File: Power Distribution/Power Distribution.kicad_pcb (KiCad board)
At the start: 16 copper layers, 20 parts, among them IC3 PCM5102 Audio Stereo DAC

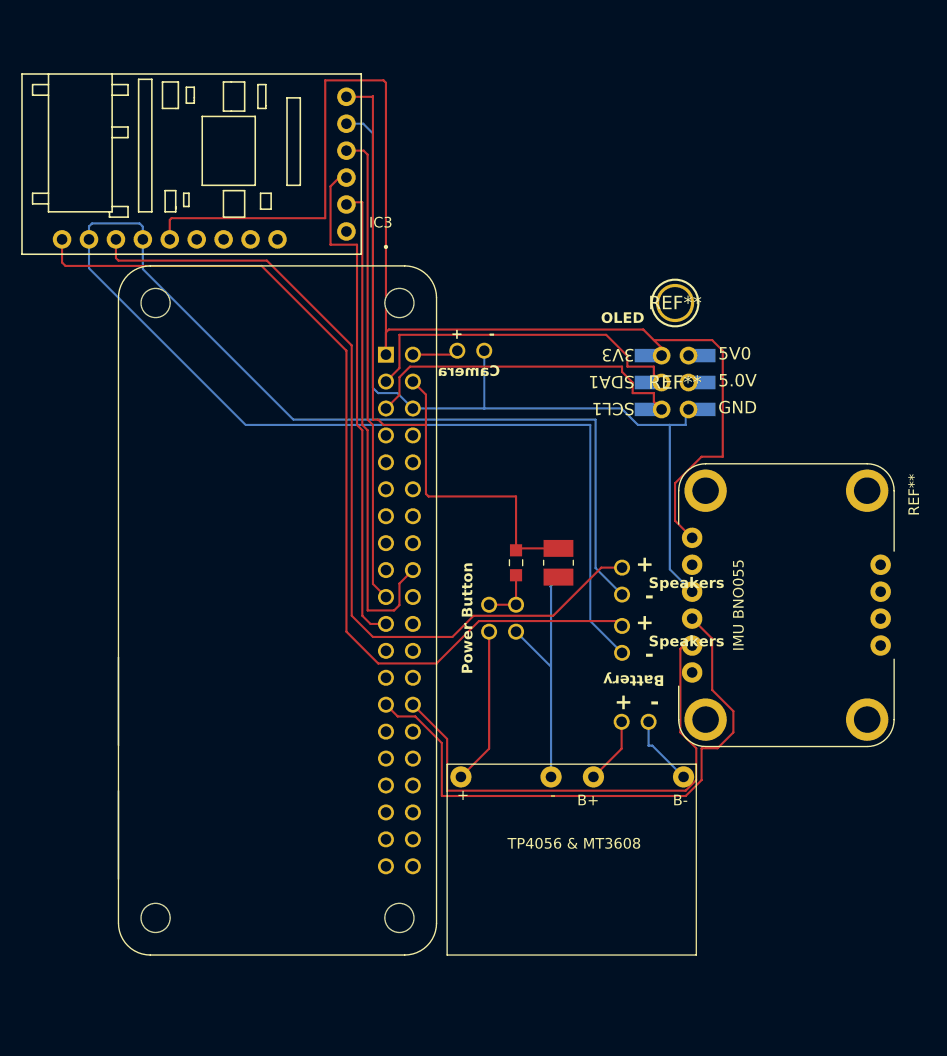
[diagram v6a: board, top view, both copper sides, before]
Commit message: Made it more compact
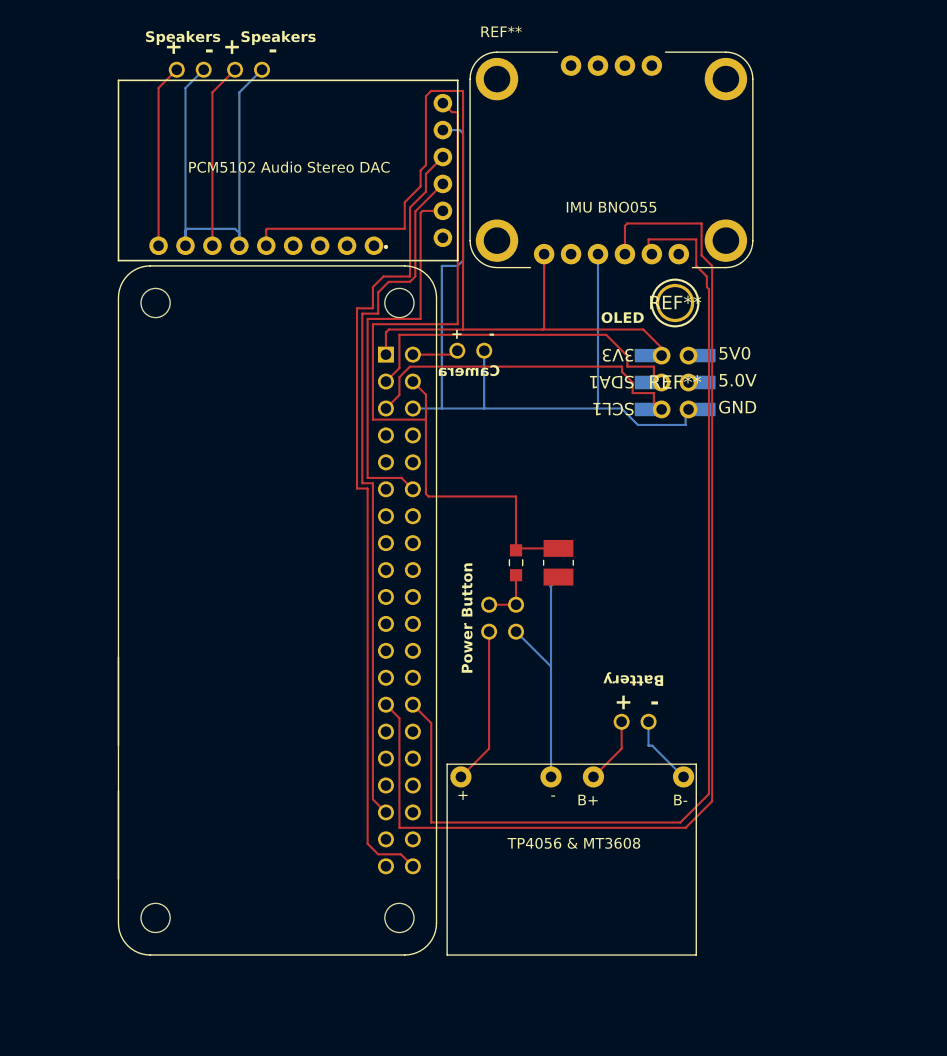
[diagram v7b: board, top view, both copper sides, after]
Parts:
- moved ? 64.6 mm to (94.0, 28.5), turned to 90 degrees
- moved ? 63.9 mm to (91.5, 28.5), turned to 90 degrees
- moved ? 63.3 mm to (88.5, 28.5), turned to 90 degrees
- moved ? 63.0 mm to (86.0, 28.5), turned to 90 degrees
- moved REF** 45.1 mm to (127.0, 37.0), turned to 0 degrees
- moved IC3 9.12 mm to (104.6, 45.1)
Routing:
- net (no net): track 962.3 -> 830.5 mm

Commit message: Made it more compact
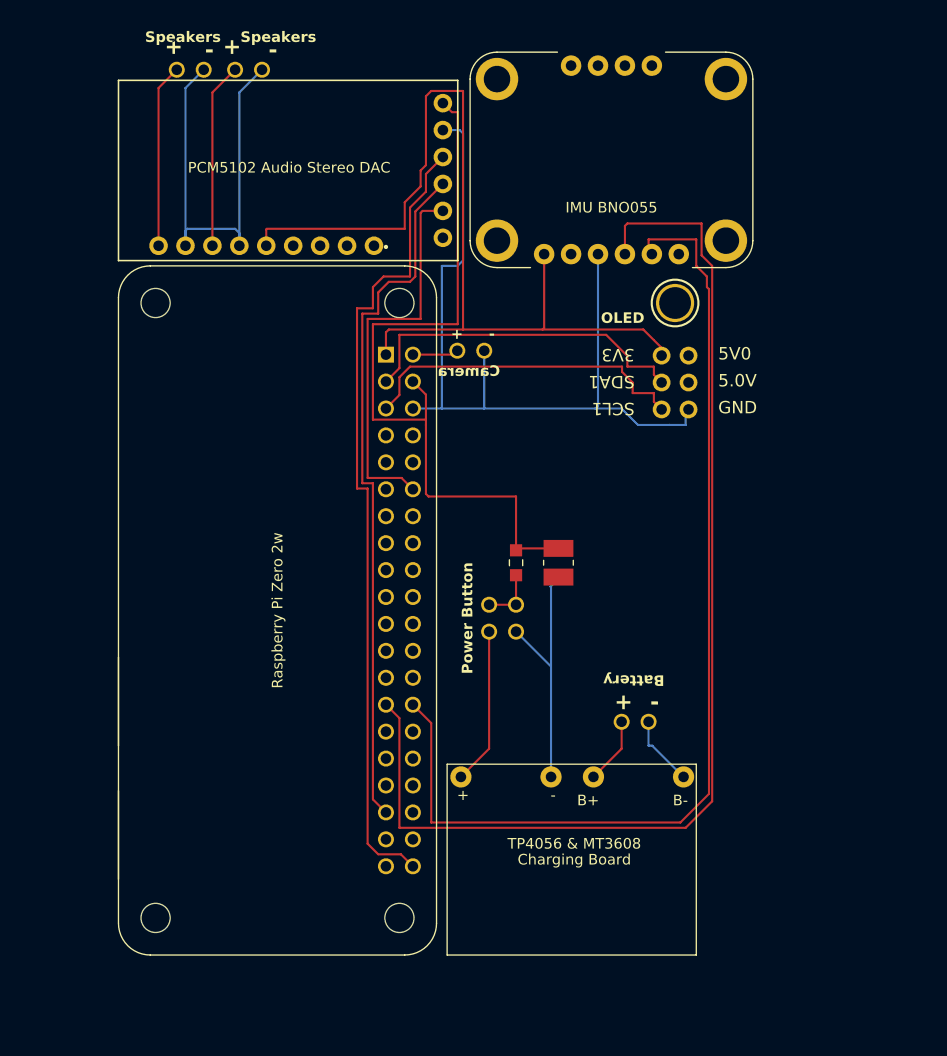
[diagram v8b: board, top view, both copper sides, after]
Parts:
- REF**: value (none) -> Val**
